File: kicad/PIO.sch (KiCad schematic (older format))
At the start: 12 parts, among them J1 Conn_02x08_Odd_Even, J2 KMDGX-6S-BS, U15 Z84C20, U16 74AHC08, U18 74HC164, U19 74HC164, U2 74AHC14

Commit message: Update to Kicad 5
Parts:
- C25, C28, C29: symbol C -> Device:C
- J1: symbol Conn_02x08_Odd_Even -> Connector_Generic:Conn_02x08_Odd_Even
- J2: symbol KMDGX-6S-BS -> headquarters:KMDGX-6S-BS
- R30, R31: symbol R -> Device:R
- U15: symbol Z84C20 -> headquarters:Z84C20
- U16: symbol 74LS08 -> 74xx:74LS08
- U18, U19: symbol 74HC164 -> headquarters:74HC164
- U2: symbol 74HC14 -> 74xx:74HC14
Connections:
- wire segments 107 -> 127
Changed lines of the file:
@@
-EESchema Schematic File Version 2
-LIBS:power
-LIBS:device
-LIBS:transistors
-LIBS:conn
-LIBS:linear
-LIBS:regul
-LIBS:74xx
-LIBS:cmos4000
-LIBS:adc-dac
-LIBS:memory
-LIBS:xilinx
-LIBS:microcontrollers
-LIBS:dsp
-LIBS:microchip
-LIBS:analog_switches
-LIBS:motorola
-LIBS:texas
-LIBS:intel
-LIBS:audio
-LIBS:interface
-LIBS:digital-audio
-LIBS:philips
-LIBS:display
-LIBS:cypress
-LIBS:siliconi
-LIBS:opto
-LIBS:atmel
-LIBS:contrib
-LIBS:valves
-LIBS:Zilog
-LIBS:Oscillators
-LIBS:switches
-LIBS:headquarters
+EESchema Schematic File Version 4
 LIBS:z80-cache
-EELAYER 25 0
+EELAYER 26 0
 EELAYER END
 $Descr USLetter 11000 8500
@@
 $EndDescr
 $Comp
-L Z84C20 U15
+L headquarters:Z84C20 U15
 U 1 1 59D82949
 P 3400 3000
@@
 ~RESET
 $Comp
-L GND #PWR055
+L power:GND #PWR055
 U 1 1 59D82A6F
 P 3400 4500
@@
 $EndComp
 $Comp
-L VCC #PWR056
+L power:VCC #PWR056
 U 1 1 59D82A86
 P 3400 1800
@@
 $EndComp
 $Comp
-L 74LS08 U16
+L 74xx:74LS08 U16
 U 1 1 59D86E33
 P 1850 2400
@@
 	2800 2800 2650 2800
 Wire Bus Line
-	2550 1900 2550 2700
-Wire Bus Line
 	2550 1900 1500 1900
-Wire Wire Line
-	1200 2300 1250 2300
-Wire Wire Line
-	1200 2500 1250 2500
 Wire Wire Line
 	2450 2400 2450 3100
@@
 NoConn ~ 4000 4100
 $Comp
-L VCC #PWR057
+L power:VCC #PWR057
 U 1 1 59D87E9E
 P 4100 3050
@@
 $EndComp
 $Comp
-L VCC #PWR058
+L power:VCC #PWR058
 U 1 1 59D87EBB
 P 4100 4200
@@
 	4000 4200 4100 4200
 Wire Wire Line
-	4000 2200 4350 2200
-Wire Wire Line
-	4000 2300 4350 2300
-Wire Wire Line
-	4000 2400 4350 2400
-Wire Wire Line
-	4000 2500 4350 2500
-Wire Wire Line
-	4000 2600 4350 2600
-Wire Wire Line
-	4000 2700 4350 2700
-Wire Wire Line
-	4000 2800 4350 2800
+	4000 2200 4050 2200
+Wire Wire Line
+	4000 2300 4100 2300
+Wire Wire Line
+	4000 2400 4150 2400
+Wire Wire Line
+	4000 2500 4200 2500
+Wire Wire Line
+	4000 2600 4250 2600
+Wire Wire Line
+	4000 2700 4250 2700
+Wire Wire Line
+	4000 2800 4300 2800
 Wire Wire Line
 	4000 3350 4950 3350
@@
 	4000 3950 5250 3950
 $Comp
-L VCC #PWR059
+L power:VCC #PWR059
 U 1 1 59D89429
 P 9400 1200
@@
 $EndComp
 $Comp
-L GND #PWR060
+L power:GND #PWR060
 U 1 1 59D8949E
 P 10200 1200
@@
 Connection ~ 4050 2200
 $Comp
-L R R30
+L Device:R R30
 U 1 1 59D8DE24
 P 9650 2700
@@
 $EndComp
 $Comp
-L VCC #PWR061
+L power:VCC #PWR061
 U 1 1 59D8DE5C
 P 9650 2550
@@
 $EndComp
 $Comp
-L R R31
+L Device:R R31
 U 1 1 59D8DE95
 P 9650 2000
@@
 $EndComp
 $Comp
-L VCC #PWR062
+L power:VCC #PWR062
 U 1 1 59D8DE9B
 P 9650 1850
@@
 $EndComp
 $Comp
-L C C25
+L Device:C C25
 U 1 1 59D929D9
 P 4700 6700
@@
 $EndComp
 $Comp
-L GND #PWR063
+L power:GND #PWR063
 U 1 1 59D929E0
 P 4450 6850
@@
 $EndComp
 $Comp
-L VCC #PWR064
+L power:VCC #PWR064
 U 1 1 59D929ED
 P 4450 6550
@@
 Connection ~ 4700 6850
 Wire Wire Line
-	4450 6550 5400 6550
-Wire Wire Line
-	4450 6850 5400 6850
+	4450 6550 4700 6550
+Wire Wire Line
+	4450 6850 4700 6850
 Text Label 6150 1550 0    60   ~ 0
 ~SRCLR
 $Comp
-L 74HC164 U18
+L headquarters:74HC164 U18
 U 1 1 59DC0329
 P 7350 2600
@@
 $EndComp
 $Comp
-L 74HC164 U19
+L headquarters:74HC164 U19
 U 1 1 59DC048A
 P 7350 3850
@@
 	6800 3150 7900 3150
 Wire Wire Line
-	7900 3150 7900 3550
+	7900 3150 7900 3400
 Connection ~ 7900 3400
 Wire Wire Line
 	7900 2700 8300 2700
 Wire Wire Line
-	8300 1550 8300 3950
+	8300 1550 8300 2700
 Wire Wire Line
 	8300 3950 7900 3950
@@
 SR7
 $Comp
-L C C28
+L Device:C C28
 U 1 1 59DC1842
 P 5050 6700
@@
 Near\nU18
 $Comp
-L C C29
+L Device:C C29
 U 1 1 59DC18A4
 P 5400 6700
@@
 Connection ~ 5050 6850
 $Comp
-L 74HC14 U2
+L 74xx:74HC14 U2
 U 5 1 59DD62A4
 P 9100 2150
@@
 	8400 1400 4100 1400
 $Comp
-L 74HC14 U2
+L 74xx:74HC14 U2
 U 6 1 59E8C9A6
 P 9100 2850
@@
 Connection ~ 8400 2150
 Wire Wire Line
-	8500 1100 8500 4100
+	8500 1100 8500 2850
 Connection ~ 8500 2850
 Wire Wire Line
@@
 Connection ~ 7900 2150
 $Comp
-L Conn_02x08_Odd_Even J1
+L Connector_Generic:Conn_02x08_Odd_Even J1
 U 1 1 5AC4F378
 P 4550 2400
@@
 $EndComp
 $Comp
-L KMDGX-6S-BS J2
+L headquarters:KMDGX-6S-BS J2
 U 1 1 5AC532E0
 P 9800 1200
@@
 $EndComp
 $Comp
-L GND #PWR065
+L power:GND #PWR065
 U 1 1 5AC53539
 P 9950 1650
@@
 Wire Wire Line
 	10100 2150 10100 1300
-Wire Wire Line
-	9550 2150 10100 2150
 Connection ~ 9650 2150
 Wire Wire Line
-	7900 2850 8650 2850
-Wire Wire Line
-	7900 2150 8650 2150
+	7900 2850 8500 2850
+Wire Wire Line
+	7900 2150 8400 2150
 Wire Wire Line
 	10100 1100 10350 1100
 Wire Wire Line
-	10350 850  10350 2850
-Wire Wire Line
-	10350 2850 9550 2850
+	10350 850  10350 1100
+Wire Wire Line
+	10350 2850 9650 2850
 Connection ~ 9650 2850
 Wire Wire Line
@@
 	4300 4900 1500 4900
 Connection ~ 4300 2800
+Wire Wire Line
+	4050 2200 4350 2200
+Wire Wire Line
+	4700 6550 5050 6550
+Wire Wire Line
+	4700 6850 5050 6850
+Wire Wire Line
+	7900 3400 7900 3550
+Wire Wire Line
+	4100 2300 4350 2300
+Wire Wire Line
+	8300 2700 8300 3950
+Wire Wire Line
+	4150 2400 4350 2400
+Wire Wire Line
+	4200 2500 4350 2500
+Wire Wire Line
+	5050 6550 5400 6550
+Wire Wire Line
+	5050 6850 5400 6850
+Wire Wire Line
+	4250 2600 4350 2600
+Wire Wire Line
+	8500 2850 8500 4100
+Wire Wire Line
+	9650 2150 10100 2150
+Wire Wire Line
+	10350 1100 10350 2850
+Wire Wire Line
+	4250 2700 4350 2700
+Wire Wire Line
+	4300 2800 4350 2800
+Wire Wire Line
+	8400 2150 8800 2150
+Wire Wire Line
+	9400 2150 9650 2150
+Wire Wire Line
+	9400 2850 9650 2850
+Wire Wire Line
+	8500 2850 8800 2850
+Wire Wire Line
+	1200 2300 1550 2300
+Wire Wire Line
+	1200 2500 1550 2500
+Wire Wire Line
+	2450 2400 2150 2400
+Wire Bus Line
+	2550 1900 2550 2700
 $EndSCHEMATC

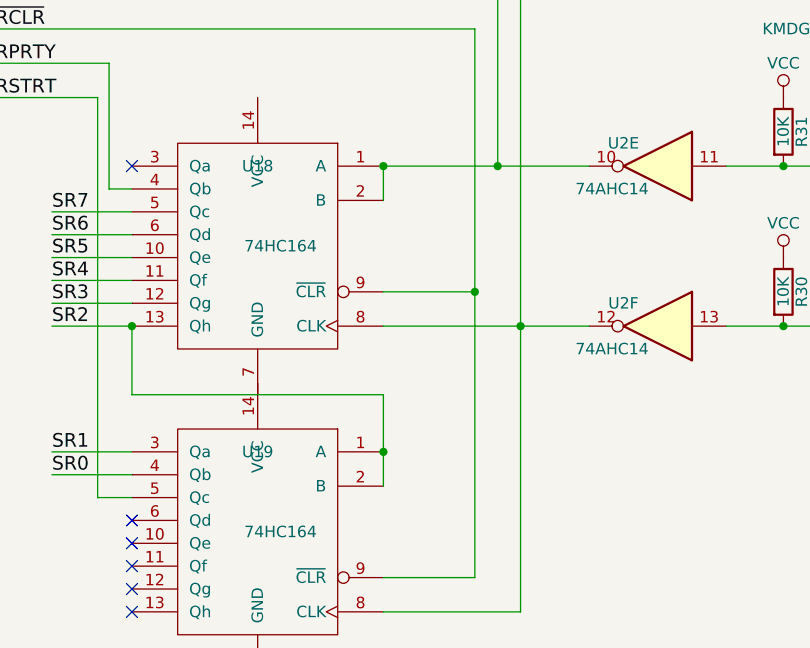
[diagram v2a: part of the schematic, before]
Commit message: SDcard interface mostly complete.
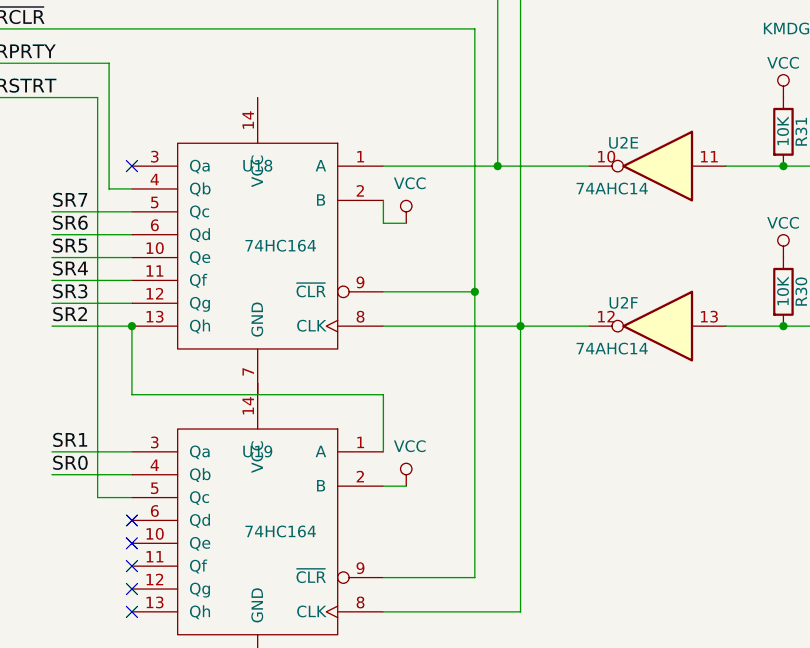
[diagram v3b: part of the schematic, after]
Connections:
- net SR2: no longer U19.2 (B)
- net VCC: now also U18.2 (B), U19.2 (B)
- net ~KDAT: no longer U18.2 (B)
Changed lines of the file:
@@
 Wire Wire Line
 	7900 3150 7900 3400
-Connection ~ 7900 3400
 Wire Wire Line
 	7900 2700 8300 2700
@@
 	8500 1100 8500 2850
 Connection ~ 8500 2850
-Wire Wire Line
-	7900 2300 7900 2150
-Connection ~ 7900 2150
 $Comp
 L Connector_Generic:Conn_02x08_Odd_Even J1
@@
 	4700 6850 5050 6850
 Wire Wire Line
-	7900 3400 7900 3550
-Wire Wire Line
 	4100 2300 4350 2300
 Wire Wire Line
@@
 Wire Wire Line
 	2450 2400 2150 2400
+$Comp
+L power:VCC #PWR073
+U 1 1 5CD73BD7
+P 8000 3550
+F 0 "#PWR073" H 8000 3400 50  0001 C CNN
+F 1 "VCC" H 8017 3723 50  0000 C CNN
+F 2 "" H 8000 3550 50  0001 C CNN
+F 3 "" H 8000 3550 50  0001 C CNN
+	1    8000 3550
+	1    0    0    -1
+$EndComp
+Wire Wire Line
+	7900 3550 8000 3550
+$Comp
+L power:VCC #PWR033
+U 1 1 5CD78C55
+P 8000 2400
+F 0 "#PWR033" H 8000 2250 50  0001 C CNN
+F 1 "VCC" H 8017 2573 50  0000 C CNN
+F 2 "" H 8000 2400 50  0001 C CNN
+F 3 "" H 8000 2400 50  0001 C CNN
+	1    8000 2400
+	1    0    0    -1
+$EndComp
+Wire Wire Line
+	7900 2300 7900 2400
+Wire Wire Line
+	7900 2400 8000 2400
 Wire Bus Line
 	2550 1900 2550 2700

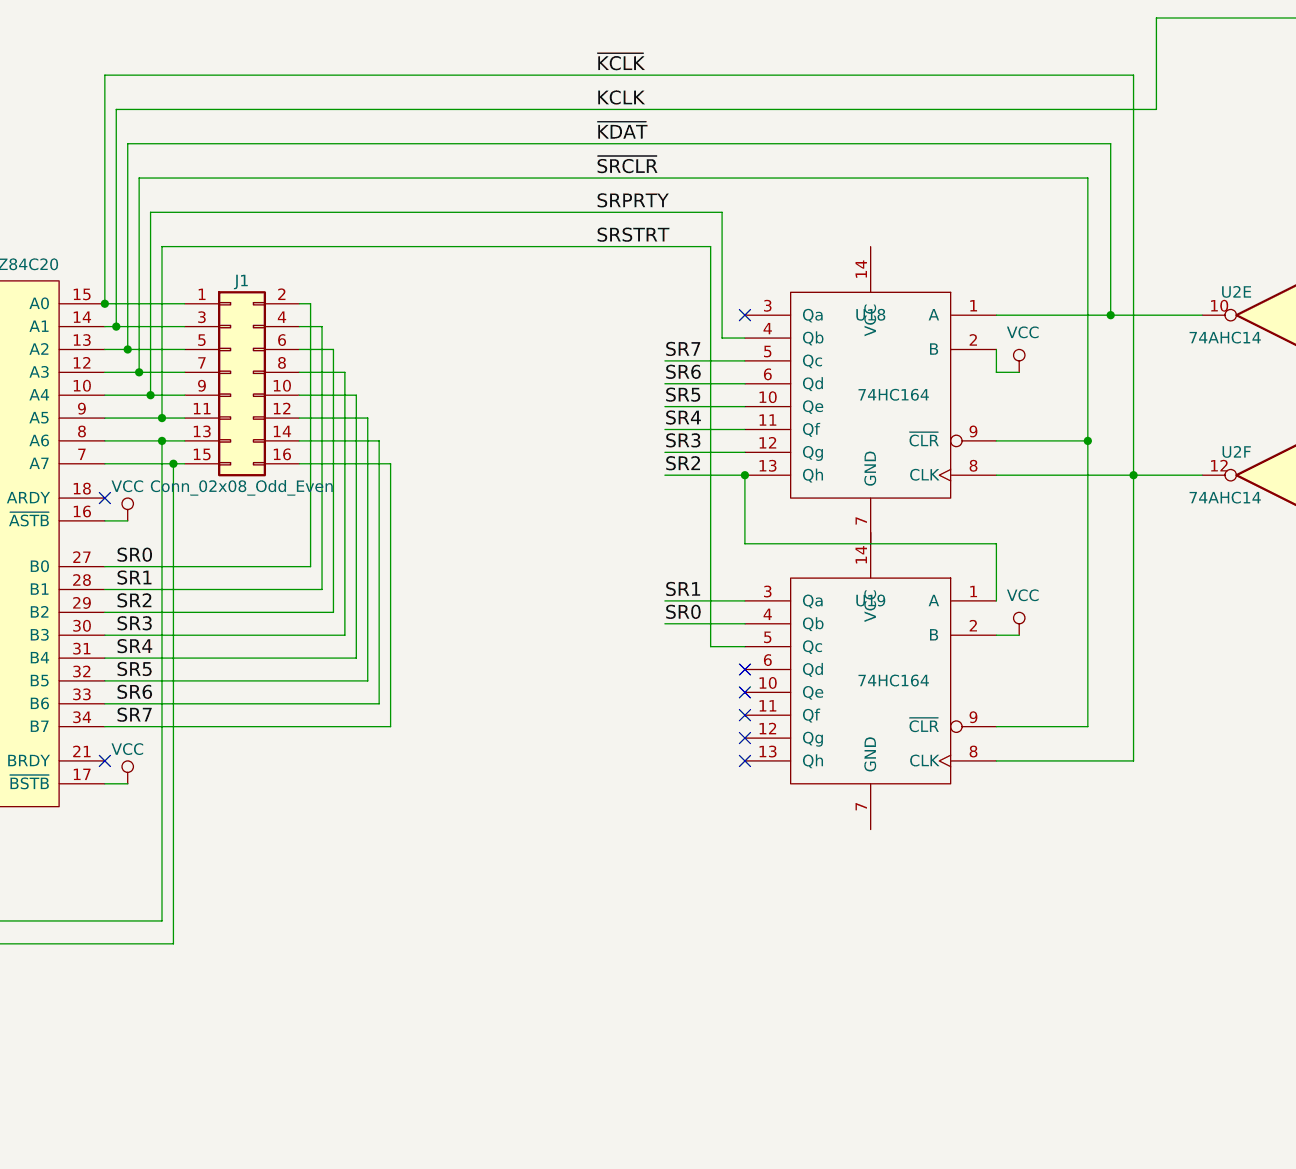
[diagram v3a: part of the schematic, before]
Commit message: Add audio output.
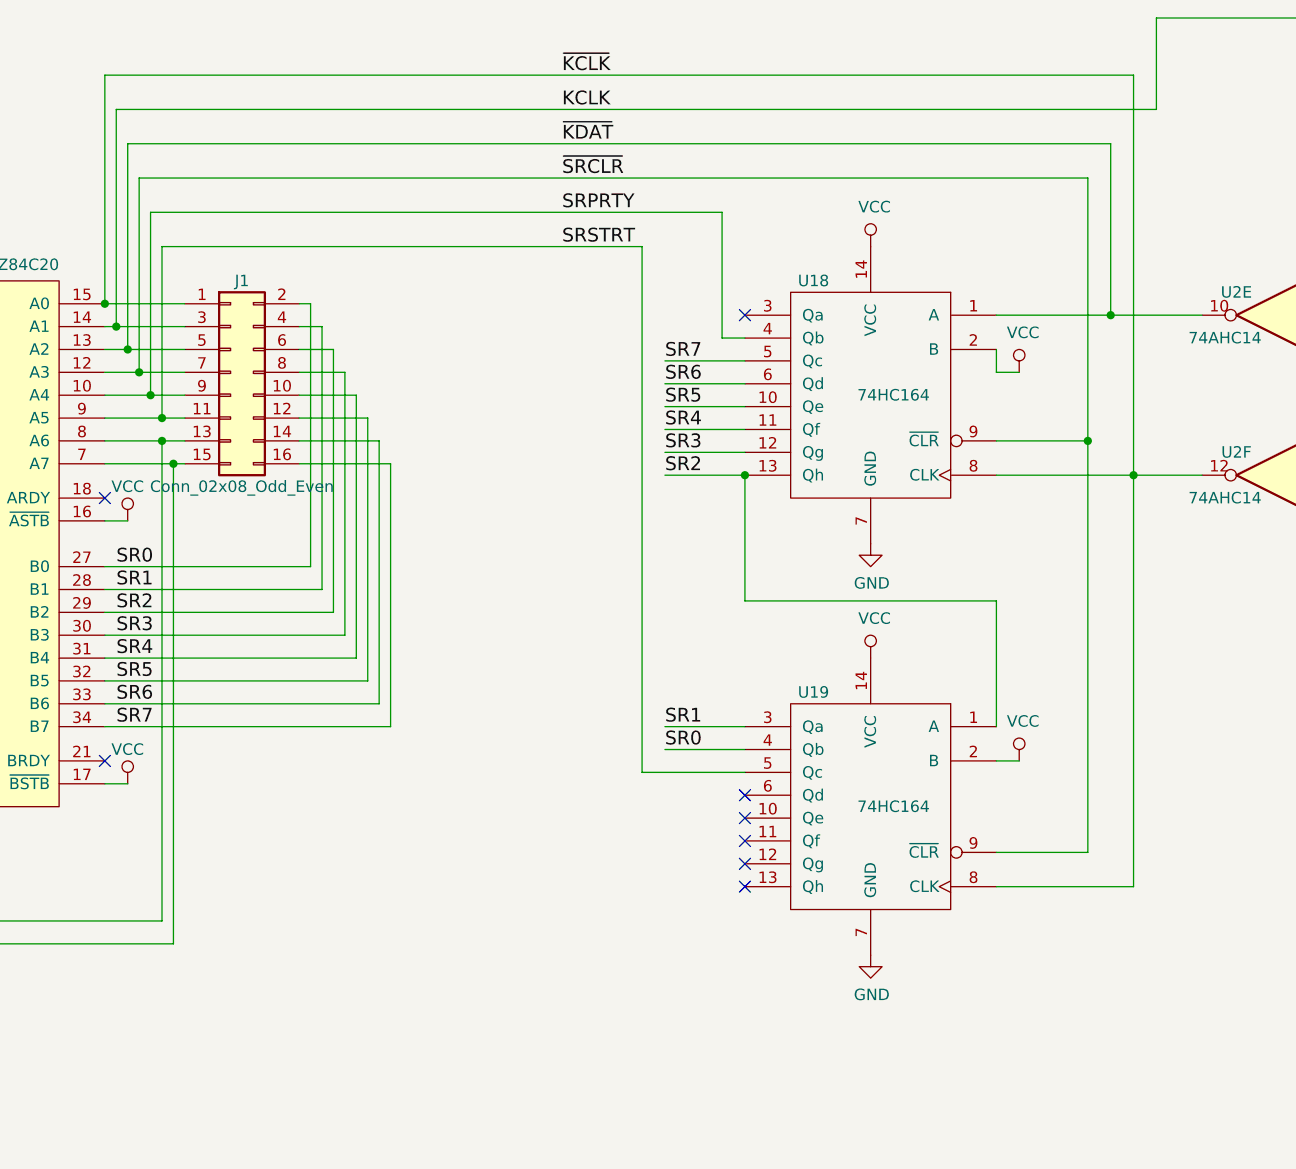
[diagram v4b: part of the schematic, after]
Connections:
- net GND: now also U18.7 (GND), U19.7 (GND)
- net VCC: now also U18.14 (VCC), U19.14 (VCC)
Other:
- moved on the sheet: U19
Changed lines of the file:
@@
 EESchema Schematic File Version 4
 LIBS:z80-cache
-EELAYER 26 0
+EELAYER 29 0
 EELAYER END
 $Descr USLetter 11000 8500
 encoding utf-8
-Sheet 5 10
+Sheet 5 11
 Title "PIO, PS/2 Keyboard Port"
 Date "2018-07-20"
@@
 	1    0    0    -1
 $EndComp
-Text Label 6150 1100 0    60   ~ 0
+Text Label 6000 1100 0    60   ~ 0
 ~KCLK
-Text Label 6150 1400 0    60   ~ 0
+Text Label 6000 1400 0    60   ~ 0
 ~KDAT
 Wire Wire Line
@@
 Wire Wire Line
 	4450 6850 4700 6850
-Text Label 6150 1550 0    60   ~ 0
+Text Label 6000 1550 0    60   ~ 0
 ~SRCLR
 $Comp
@@
 U 1 1 59DC0329
 P 7350 2600
-F 0 "U18" H 7350 3050 50  0000 C CNN
+F 0 "U18" H 7600 3200 50  0000 C CNN
 F 1 "74HC164" H 7250 2700 50  0000 C CNN
 F 2 "Housings_DIP:DIP-14_W7.62mm_LongPads" H 7200 2750 50  0001 C CNN
@@
 L headquarters:74HC164 U19
 U 1 1 59DC048A
-P 7350 3850
-F 0 "U19" H 7350 4300 50  0000 C CNN
-F 1 "74HC164" H 7250 3950 50  0000 C CNN
-F 2 "Housings_DIP:DIP-14_W7.62mm_LongPads" H 7200 4000 50  0001 C CNN
-F 3 "" H 7200 4000 50  0001 C CNN
-	1    7350 3850
+P 7350 4400
+F 0 "U19" H 7600 5000 50  0000 C CNN
+F 1 "74HC164" H 7250 4500 50  0000 C CNN
+F 2 "Housings_DIP:DIP-14_W7.62mm_LongPads" H 7200 4550 50  0001 C CNN
+F 3 "" H 7200 4550 50  0001 C CNN
+	1    7350 4400
 	-1   0    0    -1
 $EndComp
 Wire Wire Line
-	8500 4100 7900 4100
-Wire Wire Line
-	6800 2850 6800 3150
-Wire Wire Line
-	6800 3150 7900 3150
-Wire Wire Line
-	7900 3150 7900 3400
+	8500 4650 7900 4650
 Wire Wire Line
 	7900 2700 8300 2700
@@
 	8300 1550 8300 2700
 Wire Wire Line
-	8300 3950 7900 3950
+	8300 4500 7900 4500
 Wire Wire Line
 	8300 1550 4150 1550
@@
 Connection ~ 8300 2700
 Wire Wire Line
-	6650 3600 6800 3600
+	6350 4150 6800 4150
 Connection ~ 4150 2400
 Wire Wire Line
@@
 	6700 1700 4200 1700
 Wire Wire Line
-	6650 3600 6650 1850
-Wire Wire Line
-	6650 1850 4250 1850
+	6350 1850 4250 1850
 Connection ~ 4200 2500
-Text Label 6150 1700 0    60   ~ 0
+Text Label 6000 1700 0    60   ~ 0
 SRPRTY
-Text Label 6150 1850 0    60   ~ 0
+Text Label 6000 1850 0    60   ~ 0
 SRSTRT
-NoConn ~ 6800 4100
-NoConn ~ 6800 4000
-NoConn ~ 6800 3900
-NoConn ~ 6800 3800
-NoConn ~ 6800 3700
+NoConn ~ 6800 4650
+NoConn ~ 6800 4550
+NoConn ~ 6800 4450
+NoConn ~ 6800 4350
+NoConn ~ 6800 4250
 NoConn ~ 6800 2150
 Wire Wire Line
-	6450 3500 6800 3500
-Wire Wire Line
-	6450 3400 6800 3400
+	6450 4050 6800 4050
+Wire Wire Line
+	6450 3950 6800 3950
 Wire Wire Line
 	6450 2850 6800 2850
@@
 Text Label 6450 2850 0    60   ~ 0
 SR2
-Text Label 6450 3400 0    60   ~ 0
+Text Label 6450 3950 0    60   ~ 0
 SR1
-Text Label 6450 3500 0    60   ~ 0
+Text Label 6450 4050 0    60   ~ 0
 SR0
 Text Label 4050 3250 0    60   ~ 0
@@
 	8600 1250 4050 1250
 Connection ~ 4250 2600
-Text Label 6150 1250 0    60   ~ 0
+Text Label 6000 1250 0    60   ~ 0
 KCLK
 Wire Wire Line
@@
 	4100 2300 4350 2300
 Wire Wire Line
-	8300 2700 8300 3950
-Wire Wire Line
 	4150 2400 4350 2400
 Wire Wire Line
@@
 Wire Wire Line
 	4250 2600 4350 2600
-Wire Wire Line
-	8500 2850 8500 4100
 Wire Wire Line
 	9650 2150 10100 2150
@@
 L power:VCC #PWR073
 U 1 1 5CD73BD7
-P 8000 3550
-F 0 "#PWR073" H 8000 3400 50  0001 C CNN
-F 1 "VCC" H 8017 3723 50  0000 C CNN
-F 2 "" H 8000 3550 50  0001 C CNN
-F 3 "" H 8000 3550 50  0001 C CNN
-	1    8000 3550
-	1    0    0    -1
-$EndComp
-Wire Wire Line
-	7900 3550 8000 3550
+P 8000 4100
+F 0 "#PWR073" H 8000 3950 50  0001 C CNN
+F 1 "VCC" H 8017 4273 50  0000 C CNN
+F 2 "" H 8000 4100 50  0001 C CNN
+F 3 "" H 8000 4100 50  0001 C CNN
+	1    8000 4100
+	1    0    0    -1
+$EndComp
+Wire Wire Line
+	7900 4100 8000 4100
 $Comp
 L power:VCC #PWR033
@@
 Wire Wire Line
 	7900 2400 8000 2400
+$Comp
+L power:VCC #PWR0137
+U 1 1 5CBD4968
+P 7350 1850
+F 0 "#PWR0137" H 7350 1700 50  0001 C CNN
+F 1 "VCC" H 7367 2023 50  0000 C CNN
+F 2 "" H 7350 1850 50  0001 C CNN
+F 3 "" H 7350 1850 50  0001 C CNN
+	1    7350 1850
+	1    0    0    -1
+$EndComp
+$Comp
+L power:GND #PWR0140
+U 1 1 5CBD4E04
+P 7350 4950
+F 0 "#PWR0140" H 7350 4700 50  0001 C CNN
+F 1 "GND" H 7355 4777 50  0000 C CNN
+F 2 "" H 7350 4950 50  0001 C CNN
+F 3 "" H 7350 4950 50  0001 C CNN
+	1    7350 4950
+	1    0    0    -1
+$EndComp
+Wire Wire Line
+	6350 1850 6350 4150
+Wire Wire Line
+	8300 2700 8300 4500
+Wire Wire Line
+	8500 2850 8500 4650
+Wire Wire Line
+	6800 3400 7900 3400
+Wire Wire Line
+	6800 2850 6800 3400
+Wire Wire Line
+	7900 3400 7900 3950
 Wire Bus Line
 	2550 1900 2550 2700
+$Comp
+L power:GND #PWR0138
+U 1 1 5CBF9406
+P 7350 3150
+F 0 "#PWR0138" H 7350 2900 50  0001 C CNN
+F 1 "GND" H 7355 2977 50  0000 C CNN
+F 2 "" H 7350 3150 50  0001 C CNN
+F 3 "" H 7350 3150 50  0001 C CNN
+	1    7350 3150
+	1    0    0    -1
+$EndComp
+$Comp
+L power:VCC #PWR0139
+U 1 1 5CBF9840
+P 7350 3650
+F 0 "#PWR0139" H 7350 3500 50  0001 C CNN
+F 1 "VCC" H 7367 3823 50  0000 C CNN
+F 2 "" H 7350 3650 50  0001 C CNN
+F 3 "" H 7350 3650 50  0001 C CNN
+	1    7350 3650
+	1    0    0    -1
+$EndComp
 $EndSCHEMATC
